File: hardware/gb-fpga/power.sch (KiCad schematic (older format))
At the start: 31 parts, among them J3 BAT+, J4 BAT-, Q1 MBT3904DW1, SW1 SW_SPST, U4 LTC3555

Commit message: Switch from 0603 to 0402 footprints
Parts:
- C11, C3, C4, C5, C6, C7, C8, C9: footprint Capacitor_SMD:C_0603_1608Metric -> Capacitor_SMD:C_0402_1005Metric
- L1, L2, L3, L4: footprint Inductor_SMD:L_0603_1608Metric -> Inductor_SMD:L_0402_1005Metric
- R18, R19, R20, R21, R22, R23, R24, R25, R26, R27, R28, R29, R30, R31: footprint Resistor_SMD:R_0603_1608Metric -> Resistor_SMD:R_0402_1005Metric
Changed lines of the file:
@@
 F 0 "R18" H 3259 4596 50  0000 L CNN
 F 1 "3k" H 3259 4505 50  0000 L CNN
-F 2 "Resistor_SMD:R_0603_1608Metric" H 3200 4550 50  0001 C CNN
+F 2 "Resistor_SMD:R_0402_1005Metric" H 3200 4550 50  0001 C CNN
 F 3 "~" H 3200 4550 50  0001 C CNN
 	1    3200 4550
@@
 F 0 "C3" H 2950 4600 50  0000 R CNN
 F 1 "470nF" H 2950 4500 50  0000 R CNN
-F 2 "Capacitor_SMD:C_0603_1608Metric" H 3050 4550 50  0001 C CNN
+F 2 "Capacitor_SMD:C_0402_1005Metric" H 3050 4550 50  0001 C CNN
 F 3 "~" H 3050 4550 50  0001 C CNN
 	1    3050 4550
@@
 F 0 "R19" H 3659 4796 50  0000 L CNN
 F 1 "2k" H 3659 4705 50  0000 L CNN
-F 2 "Resistor_SMD:R_0603_1608Metric" H 3600 4750 50  0001 C CNN
+F 2 "Resistor_SMD:R_0402_1005Metric" H 3600 4750 50  0001 C CNN
 F 3 "~" H 3600 4750 50  0001 C CNN
 	1    3600 4750
@@
 F 0 "L1" V 5900 3750 50  0000 L CNN
 F 1 "1.5µH" V 5900 3450 50  0000 L CNN
-F 2 "Inductor_SMD:L_0603_1608Metric" H 5800 3700 50  0001 C CNN
+F 2 "Inductor_SMD:L_0402_1005Metric" H 5800 3700 50  0001 C CNN
 F 3 "~" H 5800 3700 50  0001 C CNN
 	1    5800 3700
@@
 F 0 "C4" H 6092 3846 50  0000 L CNN
 F 1 "20pF" H 6092 3755 50  0000 L CNN
-F 2 "Capacitor_SMD:C_0603_1608Metric" H 6000 3800 50  0001 C CNN
+F 2 "Capacitor_SMD:C_0402_1005Metric" H 6000 3800 50  0001 C CNN
 F 3 "~" H 6000 3800 50  0001 C CNN
 	1    6000 3800
@@
 F 0 "R20" H 6459 3846 50  0000 L CNN
 F 1 "30k" H 6459 3755 50  0000 L CNN
-F 2 "Resistor_SMD:R_0603_1608Metric" H 6400 3800 50  0001 C CNN
+F 2 "Resistor_SMD:R_0402_1005Metric" H 6400 3800 50  0001 C CNN
 F 3 "~" H 6400 3800 50  0001 C CNN
 	1    6400 3800
@@
 F 0 "R21" V 6800 3800 50  0000 L CNN
 F 1 "120k" V 6800 3950 50  0000 L CNN
-F 2 "Resistor_SMD:R_0603_1608Metric" H 6700 3900 50  0001 C CNN
+F 2 "Resistor_SMD:R_0402_1005Metric" H 6700 3900 50  0001 C CNN
 F 3 "~" H 6700 3900 50  0001 C CNN
 	1    6700 3900
@@
 F 0 "C5" H 6942 3846 50  0000 L CNN
 F 1 "22µF" H 6942 3755 50  0000 L CNN
-F 2 "Capacitor_SMD:C_0603_1608Metric" H 6850 3800 50  0001 C CNN
+F 2 "Capacitor_SMD:C_0402_1005Metric" H 6850 3800 50  0001 C CNN
 F 3 "~" H 6850 3800 50  0001 C CNN
 	1    6850 3800
@@
 F 0 "L2" V 5900 4150 50  0000 L CNN
 F 1 "3.3µH" V 5900 3850 50  0000 L CNN
-F 2 "Inductor_SMD:L_0603_1608Metric" H 5800 4100 50  0001 C CNN
+F 2 "Inductor_SMD:L_0402_1005Metric" H 5800 4100 50  0001 C CNN
 F 3 "~" H 5800 4100 50  0001 C CNN
 	1    5800 4100
@@
 F 0 "C6" H 6092 4246 50  0000 L CNN
 F 1 "20pF" H 6092 4155 50  0000 L CNN
-F 2 "Capacitor_SMD:C_0603_1608Metric" H 6000 4200 50  0001 C CNN
+F 2 "Capacitor_SMD:C_0402_1005Metric" H 6000 4200 50  0001 C CNN
 F 3 "~" H 6000 4200 50  0001 C CNN
 	1    6000 4200
@@
 F 0 "R22" H 6459 4246 50  0000 L CNN
 F 1 "150k" H 6459 4155 50  0000 L CNN
-F 2 "Resistor_SMD:R_0603_1608Metric" H 6400 4200 50  0001 C CNN
+F 2 "Resistor_SMD:R_0402_1005Metric" H 6400 4200 50  0001 C CNN
 F 3 "~" H 6400 4200 50  0001 C CNN
 	1    6400 4200
@@
 F 0 "R23" V 6800 4200 50  0000 L CNN
 F 1 "120k" V 6800 4350 50  0000 L CNN
-F 2 "Resistor_SMD:R_0603_1608Metric" H 6700 4300 50  0001 C CNN
+F 2 "Resistor_SMD:R_0402_1005Metric" H 6700 4300 50  0001 C CNN
 F 3 "~" H 6700 4300 50  0001 C CNN
 	1    6700 4300
@@
 F 0 "C7" H 6942 4246 50  0000 L CNN
 F 1 "10µF" H 6942 4155 50  0000 L CNN
-F 2 "Capacitor_SMD:C_0603_1608Metric" H 6850 4200 50  0001 C CNN
+F 2 "Capacitor_SMD:C_0402_1005Metric" H 6850 4200 50  0001 C CNN
 F 3 "~" H 6850 4200 50  0001 C CNN
 	1    6850 4200
@@
 F 0 "L3" V 5900 4550 50  0000 L CNN
 F 1 "2.2µH" V 5900 4250 50  0000 L CNN
-F 2 "Inductor_SMD:L_0603_1608Metric" H 5800 4500 50  0001 C CNN
+F 2 "Inductor_SMD:L_0402_1005Metric" H 5800 4500 50  0001 C CNN
 F 3 "~" H 5800 4500 50  0001 C CNN
 	1    5800 4500
@@
 F 0 "C8" H 6092 4646 50  0000 L CNN
 F 1 "20pF" H 6092 4555 50  0000 L CNN
-F 2 "Capacitor_SMD:C_0603_1608Metric" H 6000 4600 50  0001 C CNN
+F 2 "Capacitor_SMD:C_0402_1005Metric" H 6000 4600 50  0001 C CNN
 F 3 "~" H 6000 4600 50  0001 C CNN
 	1    6000 4600
@@
 F 0 "R24" H 6459 4646 50  0000 L CNN
 F 1 "180k" H 6459 4555 50  0000 L CNN
-F 2 "Resistor_SMD:R_0603_1608Metric" H 6400 4600 50  0001 C CNN
+F 2 "Resistor_SMD:R_0402_1005Metric" H 6400 4600 50  0001 C CNN
 F 3 "~" H 6400 4600 50  0001 C CNN
 	1    6400 4600
@@
 F 0 "R25" V 6800 4600 50  0000 L CNN
 F 1 "57.6k" V 6800 4750 50  0000 L CNN
-F 2 "Resistor_SMD:R_0603_1608Metric" H 6700 4700 50  0001 C CNN
+F 2 "Resistor_SMD:R_0402_1005Metric" H 6700 4700 50  0001 C CNN
 F 3 "~" H 6700 4700 50  0001 C CNN
 	1    6700 4700
@@
 F 0 "C9" H 6942 4646 50  0000 L CNN
 F 1 "10µF" H 6942 4555 50  0000 L CNN
-F 2 "Capacitor_SMD:C_0603_1608Metric" H 6850 4600 50  0001 C CNN
+F 2 "Capacitor_SMD:C_0402_1005Metric" H 6850 4600 50  0001 C CNN
 F 3 "~" H 6850 4600 50  0001 C CNN
 	1    6850 4600
@@
 F 0 "C11" H 6592 2996 50  0000 L CNN
 F 1 "22µF" H 6592 2905 50  0000 L CNN
-F 2 "Capacitor_SMD:C_0603_1608Metric" H 6500 2950 50  0001 C CNN
+F 2 "Capacitor_SMD:C_0402_1005Metric" H 6500 2950 50  0001 C CNN
 F 3 "~" H 6500 2950 50  0001 C CNN
 	1    6500 2950
@@
 F 0 "L4" V 5300 2800 50  0000 L CNN
 F 1 "3.3µH" V 5350 2500 50  0000 L CNN
-F 2 "Inductor_SMD:L_0603_1608Metric" H 5350 2900 50  0001 C CNN
+F 2 "Inductor_SMD:L_0402_1005Metric" H 5350 2900 50  0001 C CNN
 F 3 "~" H 5350 2900 50  0001 C CNN
 	1    5350 2900
@@
 F 0 "R26" H 1659 3746 50  0000 L CNN
 F 1 "10k" H 1659 3655 50  0000 L CNN
-F 2 "Resistor_SMD:R_0603_1608Metric" H 1600 3700 50  0001 C CNN
+F 2 "Resistor_SMD:R_0402_1005Metric" H 1600 3700 50  0001 C CNN
 F 3 "~" H 1600 3700 50  0001 C CNN
 	1    1600 3700
@@
 F 0 "R28" H 2559 3946 50  0000 L CNN
 F 1 "10k" H 2559 3855 50  0000 L CNN
-F 2 "Resistor_SMD:R_0603_1608Metric" H 2500 3900 50  0001 C CNN
+F 2 "Resistor_SMD:R_0402_1005Metric" H 2500 3900 50  0001 C CNN
 F 3 "~" H 2500 3900 50  0001 C CNN
 	1    2500 3900
@@
 F 0 "R27" V 2350 3850 50  0000 L TNN
 F 1 "3k" V 2350 3700 50  0000 L TNN
-F 2 "Resistor_SMD:R_0603_1608Metric" H 2300 3800 50  0001 C CNN
+F 2 "Resistor_SMD:R_0402_1005Metric" H 2300 3800 50  0001 C CNN
 F 3 "~" H 2300 3800 50  0001 C CNN
 	1    2300 3800
@@
 F 0 "R31" V 1350 5350 50  0000 L TNN
 F 1 "1k" V 1350 5200 50  0000 L TNN
-F 2 "Resistor_SMD:R_0603_1608Metric" H 1300 5300 50  0001 C CNN
+F 2 "Resistor_SMD:R_0402_1005Metric" H 1300 5300 50  0001 C CNN
 F 3 "~" H 1300 5300 50  0001 C CNN
 	1    1300 5300
@@
 F 0 "R29" V 2050 4550 50  0000 L TNN
 F 1 "30k" V 2050 4400 50  0000 L TNN
-F 2 "Resistor_SMD:R_0603_1608Metric" H 2000 4500 50  0001 C CNN
+F 2 "Resistor_SMD:R_0402_1005Metric" H 2000 4500 50  0001 C CNN
 F 3 "~" H 2000 4500 50  0001 C CNN
 	1    2000 4500
@@
 F 0 "R30" H 1750 4700 50  0000 R CNN
 F 1 "30k" H 1750 4600 50  0000 R CNN
-F 2 "Resistor_SMD:R_0603_1608Metric" H 1800 4650 50  0001 C CNN
+F 2 "Resistor_SMD:R_0402_1005Metric" H 1800 4650 50  0001 C CNN
 F 3 "~" H 1800 4650 50  0001 C CNN
 	1    1800 4650

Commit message: Add chargeing indicator LED
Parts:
- added D3: CHRG, LED_SMD:LED_0402_1005Metric, symbol Device:LED_Small
- added R32: 200Ω, Resistor_SMD:R_0402_1005Metric, symbol Device:R_Small
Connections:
- net at C11.1, L4.2, SW1.1 (A)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: now also R32.1
- net at U4.21 (~CHRG): now also D3.1 (K)
- new net: D3.2 (A), R32.2
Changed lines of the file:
@@
 Connection ~ 6500 2800
 Wire Wire Line
-	6500 2800 5500 2800
+	6500 2800 5800 2800
 $Comp
 L Device:L_Small L4
@@
 Text GLabel 1350 4500 0    50   Input ~ 0
 VOUT
+$Comp
+L Device:LED_Small D3
+U 1 1 60DA8BD6
+P 2950 3000
+F 0 "D3" V 2996 2930 50  0000 R CNN
+F 1 "CHRG" V 2905 2930 50  0000 R CNN
+F 2 "LED_SMD:LED_0402_1005Metric" V 2950 3000 50  0001 C CNN
+F 3 "~" V 2950 3000 50  0001 C CNN
+	1    2950 3000
+	0    -1   -1   0
+$EndComp
+Wire Wire Line
+	2950 3100 3800 3100
+$Comp
+L Device:R_Small R32
+U 1 1 60DB5232
+P 2950 2650
+F 0 "R32" H 3009 2696 50  0000 L CNN
+F 1 "200Ω" H 3009 2605 50  0000 L CNN
+F 2 "Resistor_SMD:R_0402_1005Metric" H 2950 2650 50  0001 C CNN
+F 3 "~" H 2950 2650 50  0001 C CNN
+	1    2950 2650
+	1    0    0    -1
+$EndComp
+Wire Wire Line
+	2950 2750 2950 2900
+Wire Wire Line
+	2950 2550 2950 1800
+Wire Wire Line
+	2950 1800 5800 1800
+Wire Wire Line
+	5800 1800 5800 2800
+Connection ~ 5800 2800
+Wire Wire Line
+	5800 2800 5500 2800
 $EndSCHEMATC

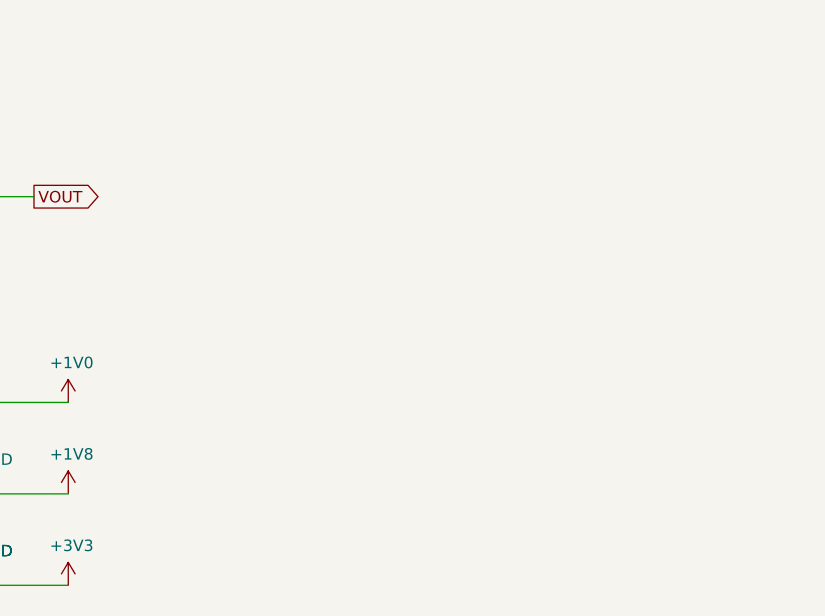
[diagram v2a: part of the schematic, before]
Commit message: Add 5V voltage regulator
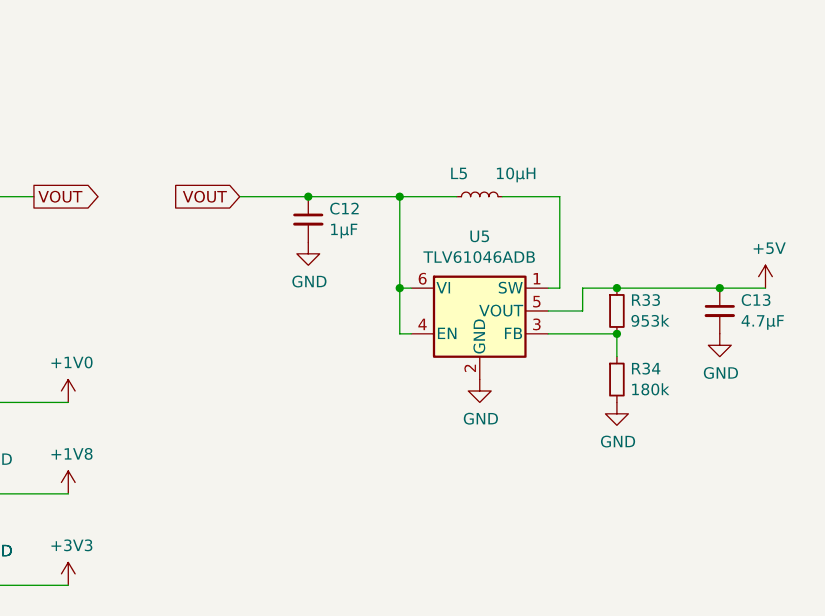
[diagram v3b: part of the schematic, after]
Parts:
- added C12: 1µF, Capacitor_SMD:C_0402_1005Metric, symbol Device:C_Small
- added C13: 4.7µF, Capacitor_SMD:C_0402_1005Metric, symbol Device:C_Small
- added L5: 10µH, Inductor_SMD:L_0402_1005Metric, symbol Device:L_Small
- added R33: 953k, Resistor_SMD:R_0402_1005Metric, symbol Device:R_Small
- added R34: 180k, Resistor_SMD:R_0402_1005Metric, symbol Device:R_Small
- added U5: TLV61046ADB, Package_TO_SOT_SMD:SOT-23-6, symbol Regulator_Switching:TLV61046ADB
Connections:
- net GND: now also C12.2, C13.2, R34.2, U5.2 (GND)
- net VOUT: now also C12.1, L5.1, U5.4 (EN), U5.6 (VI)
- new net: L5.2, U5.1 (SW)
- new net: R33.2, R34.1, U5.3 (FB)
- new net +5V: C13.1, R33.1, U5.5 (VOUT)
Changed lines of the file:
@@
 Wire Wire Line
 	5800 2800 5500 2800
+$Comp
+L Regulator_Switching:TLV61046ADB U5
+U 1 1 60DC7FC6
+P 9500 3400
+F 0 "U5" H 9500 3825 50  0000 C CNN
+F 1 "TLV61046ADB" H 9500 3734 50  0000 C CNN
+F 2 "Package_TO_SOT_SMD:SOT-23-6" H 9550 3250 50  0001 L CIN
+F 3 "http://www.ti.com/lit/ds/symlink/tlv61046a.pdf" H 9500 3500 50  0001 C CNN
+	1    9500 3400
+	1    0    0    -1
+$EndComp
+$Comp
+L Device:L_Small L5
+U 1 1 60DCDA49
+P 9500 2800
+F 0 "L5" V 9600 2850 50  0000 L CNN
+F 1 "10µH" V 9600 2550 50  0000 L CNN
+F 2 "Inductor_SMD:L_0402_1005Metric" H 9500 2800 50  0001 C CNN
+F 3 "~" H 9500 2800 50  0001 C CNN
+	1    9500 2800
+	0    -1   -1   0
+$EndComp
+Wire Wire Line
+	9800 3200 9850 3200
+Wire Wire Line
+	9850 3200 9850 2800
+Wire Wire Line
+	9850 2800 9600 2800
+Wire Wire Line
+	9400 2800 9150 2800
+Wire Wire Line
+	9150 2800 9150 3200
+Wire Wire Line
+	9150 3200 9200 3200
+Text GLabel 8450 2800 0    50   Input ~ 0
+VOUT
+Wire Wire Line
+	8450 2800 8750 2800
+Connection ~ 9150 2800
+$Comp
+L Device:C_Small C12
+U 1 1 60DDFE96
+P 8750 2900
+F 0 "C12" H 8842 2946 50  0000 L CNN
+F 1 "1µF" H 8842 2855 50  0000 L CNN
+F 2 "Capacitor_SMD:C_0402_1005Metric" H 8750 2900 50  0001 C CNN
+F 3 "~" H 8750 2900 50  0001 C CNN
+	1    8750 2900
+	1    0    0    -1
+$EndComp
+Connection ~ 8750 2800
+Wire Wire Line
+	8750 2800 9150 2800
+$Comp
+L power:GND #PWR0158
+U 1 1 60DE0AA8
+P 8750 3000
+F 0 "#PWR0158" H 8750 2750 50  0001 C CNN
+F 1 "GND" H 8755 2827 50  0000 C CNN
+F 2 "" H 8750 3000 50  0001 C CNN
+F 3 "" H 8750 3000 50  0001 C CNN
+	1    8750 3000
+	1    0    0    -1
+$EndComp
+$Comp
+L power:GND #PWR0159
+U 1 1 60DE1626
+P 9500 3600
+F 0 "#PWR0159" H 9500 3350 50  0001 C CNN
+F 1 "GND" H 9505 3427 50  0000 C CNN
+F 2 "" H 9500 3600 50  0001 C CNN
+F 3 "" H 9500 3600 50  0001 C CNN
+	1    9500 3600
+	1    0    0    -1
+$EndComp
+$Comp
+L Device:R_Small R33
+U 1 1 60DE21AA
+P 10100 3300
+F 0 "R33" H 10159 3346 50  0000 L CNN
+F 1 "953k" H 10159 3255 50  0000 L CNN
+F 2 "Resistor_SMD:R_0402_1005Metric" H 10100 3300 50  0001 C CNN
+F 3 "~" H 10100 3300 50  0001 C CNN
+	1    10100 3300
+	1    0    0    -1
+$EndComp
+$Comp
+L Device:R_Small R34
+U 1 1 60DE291A
+P 10100 3600
+F 0 "R34" H 10159 3646 50  0000 L CNN
+F 1 "180k" H 10159 3555 50  0000 L CNN
+F 2 "Resistor_SMD:R_0402_1005Metric" H 10100 3600 50  0001 C CNN
+F 3 "~" H 10100 3600 50  0001 C CNN
+	1    10100 3600
+	1    0    0    -1
+$EndComp
+$Comp
+L power:GND #PWR0160
+U 1 1 60DE2E77
+P 10100 3700
+F 0 "#PWR0160" H 10100 3450 50  0001 C CNN
+F 1 "GND" H 10105 3527 50  0000 C CNN
+F 2 "" H 10100 3700 50  0001 C CNN
+F 3 "" H 10100 3700 50  0001 C CNN
+	1    10100 3700
+	1    0    0    -1
+$EndComp
+Wire Wire Line
+	10100 3200 9950 3200
+Wire Wire Line
+	9950 3200 9950 3300
+Wire Wire Line
+	9950 3300 9800 3300
+Wire Wire Line
+	9800 3400 10100 3400
+Wire Wire Line
+	10100 3400 10100 3500
+Connection ~ 10100 3400
+Wire Wire Line
+	10100 3200 10550 3200
+Connection ~ 10100 3200
+$Comp
+L power:+5V #PWR0161
+U 1 1 60DF8CC5
+P 10750 3200
+F 0 "#PWR0161" H 10750 3050 50  0001 C CNN
+F 1 "+5V" H 10765 3373 50  0000 C CNN
+F 2 "" H 10750 3200 50  0001 C CNN
+F 3 "" H 10750 3200 50  0001 C CNN
+	1    10750 3200
+	1    0    0    -1
+$EndComp
+$Comp
+L Device:C_Small C13
+U 1 1 60DF8D06
+P 10550 3300
+F 0 "C13" H 10642 3346 50  0000 L CNN
+F 1 "4.7µF" H 10642 3255 50  0000 L CNN
+F 2 "Capacitor_SMD:C_0402_1005Metric" H 10550 3300 50  0001 C CNN
+F 3 "~" H 10550 3300 50  0001 C CNN
+	1    10550 3300
+	1    0    0    -1
+$EndComp
+Connection ~ 10550 3200
+Wire Wire Line
+	10550 3200 10750 3200
+$Comp
+L power:GND #PWR0162
+U 1 1 60DF938D
+P 10550 3400
+F 0 "#PWR0162" H 10550 3150 50  0001 C CNN
+F 1 "GND" H 10555 3227 50  0000 C CNN
+F 2 "" H 10550 3400 50  0001 C CNN
+F 3 "" H 10550 3400 50  0001 C CNN
+	1    10550 3400
+	1    0    0    -1
+$EndComp
+Wire Wire Line
+	9150 3200 9150 3400
+Wire Wire Line
+	9150 3400 9200 3400
+Connection ~ 9150 3200
 $EndSCHEMATC

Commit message: Add power switch
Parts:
- removed SW1: SW_SPST, symbol Switch:SW_SPST
- added SW1: Switch, gb-fpga:EG2215, symbol gb-fpga:Switch
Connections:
- net GND: now also SW1.4 (GND)
- net VOUT: now also SW1.3
- net at C11.1, L4.2, R32.1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: now also SW1.2
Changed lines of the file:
@@
 	1    0    0    -1
 $EndComp
-Text GLabel 7550 2800 2    50   Output ~ 0
+Text GLabel 7700 2900 2    50   Output ~ 0
 VOUT
 Wire Wire Line
-	7550 2800 7350 2800
+	7700 2900 7600 2900
 Text GLabel 1450 3600 0    50   Input ~ 0
 VOUT
@@
 	1    0    0    -1
 $EndComp
-$Comp
-L Switch:SW_SPST SW1
-U 1 1 60E48A72
-P 7150 2800
-F 0 "SW1" H 7150 3035 50  0000 C CNN
-F 1 "SW_SPST" H 7150 2944 50  0000 C CNN
-F 2 "" H 7150 2800 50  0001 C CNN
-F 3 "~" H 7150 2800 50  0001 C CNN
-	1    7150 2800
-	1    0    0    -1
-$EndComp
-Wire Wire Line
-	6950 2800 6500 2800
+Wire Wire Line
+	7100 2800 6500 2800
 Wire Wire Line
 	1600 3600 3800 3600
@@
 	9150 3400 9200 3400
 Connection ~ 9150 3200
+$Comp
+L gb-fpga:Switch SW1
+U 1 1 60DEB027
+P 7350 2800
+F 0 "SW1" H 7350 3125 50  0000 C CNN
+F 1 "Switch" H 7350 3034 50  0000 C CNN
+F 2 "gb-fpga:EG2215" H 7350 2800 50  0001 C CNN
+F 3 "" H 7350 2800 50  0001 C CNN
+	1    7350 2800
+	1    0    0    -1
+$EndComp
+$Comp
+L power:GND #PWR0185
+U 1 1 60E05727
+P 7100 2900
+F 0 "#PWR0185" H 7100 2650 50  0001 C CNN
+F 1 "GND" H 7105 2727 50  0000 C CNN
+F 2 "" H 7100 2900 50  0001 C CNN
+F 3 "" H 7100 2900 50  0001 C CNN
+	1    7100 2900
+	1    0    0    -1
+$EndComp
 $EndSCHEMATC
